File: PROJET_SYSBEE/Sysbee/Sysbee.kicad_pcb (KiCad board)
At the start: 2 copper layers, 64 x 58 mm, 47 parts, among them J1 Alim12V, J2 Connecteur Sim, J3 NO, J4 NE, J5 SO, J6 SE, J7 Connecteur programmation, J8 Micro_SD_Card_Det_Hirose_DM3AT, J9 Conn_01x03, U1 STM32L073CZTx, U2 LT1764, U3 AP1117-33, U4 ADS1231

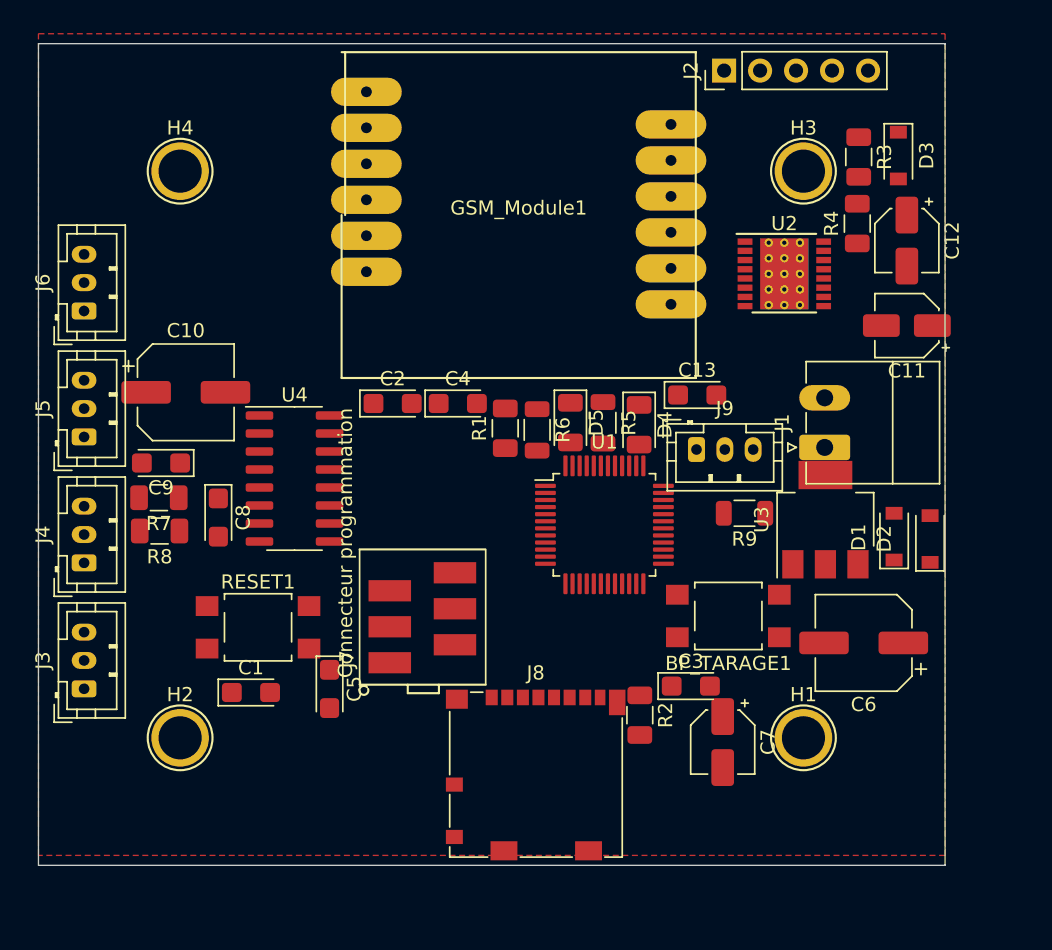
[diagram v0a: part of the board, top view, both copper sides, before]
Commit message: placement et routage, reste à redessiner un peu les pistes et rajouter les écritures F.Silks
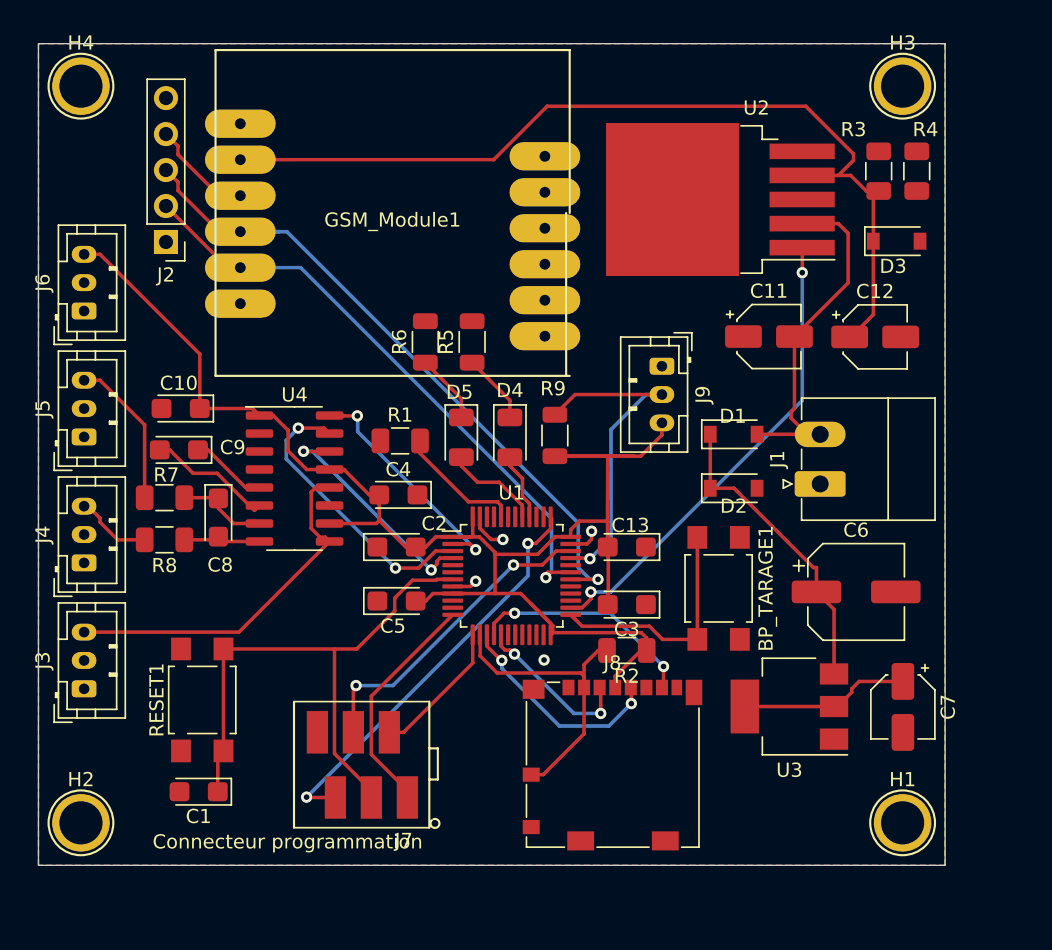
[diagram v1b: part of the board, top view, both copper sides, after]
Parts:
- C10: footprint Capacitor_SMD:CP_Elec_6.3x5.4 -> Capacitor_Tantalum_SMD:CP_EIA-3216-18_Kemet-A
- U2: value LT1764 -> MIC29302WU; footprint Package_SO:HTSSOP-16-1EP_4.4x5mm_P0.65mm_EP3.4x5mm_Mask3x3mm_ThermalVias -> Package_TO_SOT_SMD:TO-263-5_TabPin3
- moved J2 41.2 mm to (49.0, 44.0), turned to 180 degrees
- moved J7 15.9 mm to (59.7, 81.9), turned to 180 degrees
- moved R9 14.5 mm to (76.5, 57.7), turned to 90 degrees
- moved D2 14.3 mm to (89.1, 61.4), turned to 0 degrees
- moved D1 13.4 mm to (89.1, 57.6), turned to 0 degrees
- moved U3 13.4 mm to (93.0, 76.8), turned to 180 degrees
- moved C7 13.0 mm to (101.0, 76.8)
- moved C13 11.8 mm to (81.5, 65.5), turned to 180 degrees
- moved R5 10.9 mm to (70.6, 51.1), turned to 90 degrees
- moved C2 10.1 mm to (65.3, 65.5)
- moved R6 10.0 mm to (67.3, 51.1), turned to 90 degrees
- moved C11 9.76 mm to (91.6, 50.7), turned to 0 degrees
- moved H1 9.22 mm to (101.0, 85.0)
- moved H2 9.22 mm to (43.0, 85.0)
- moved H3 9.22 mm to (101.0, 33.0)
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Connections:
- C13 pad 1: Net-(C13-Pad1) -> GND
- C13 pad 2: /Alim/3,3V -> /E+
- C2 pad 1: Net-(C2-Pad1) -> GND
- C2 pad 2: /Alim/3,3V -> /E+
- C3 pad 1: Net-(C3-Pad1) -> GND
- C3 pad 2: /Alim/3,3V -> /E+
- C4 pad 1: Net-(C4-Pad1) -> GND
- C4 pad 2: /Alim/3,3V -> /E+
- C5 pad 1: Net-(C5-Pad1) -> GND
- C5 pad 2: /Alim/3,3V -> /E+
- C7 pad 1: /Alim/3,3V -> /E+
- J8 pad 4: /Alim/3,3V -> /E+
- J8 pad 7: /Microcontrôleur/SPI_MOSI -> /Microcontrôleur/SPI_MISO
- J9 pad 3: /Alim/3,3V -> /E+
- R2 pad 1: /Alim/3,3V -> /E+
- R9 pad 1: /Alim/3,3V -> /E+
- U1 pad 1: Net-(C2-Pad1) -> /E+
- U1 pad 14: /Microcontrôleur/SPI_SS -> /Microcontrôleur/SD_CS
- U1 pad 21: /Microcontrôleur/SD_CS -> Net-(U1-Pad21)
- U1 pad 24: Net-(C3-Pad1) -> /E+
- U1 pad 36: Net-(C13-Pad1) -> /E+
- U1 pad 48: Net-(C4-Pad1) -> /E+
- U1 pad 9: Net-(C5-Pad1) -> /E+
- U2 pad 1: GND -> /Alim/GSM_SHDN
- U2 pad 2: Net-(U2-Pad2) -> /Alim/12V
- U2 pad 3: /Alim/3,9V -> GND
- U2 pad 5: /Alim/3,9V -> Net-(R3-Pad2)
- U3 pad 2: /Alim/3,3V -> /E+
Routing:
- net /E+: track 0.00 -> 130.1 mm
- net /Alim/3,9V: track 0.00 -> 64.9 mm
- net /GSM_RX: track 0.00 -> 49.3 mm, vias 0 -> 1
- net /GSM_TX: track 0.00 -> 42.7 mm, vias 0 -> 1
- net /Microcontrôleur/NRST: track 0.00 -> 40.5 mm
- net /Alim/GSM_SHDN: track 0.00 -> 35.3 mm, vias 0 -> 2
- net /Microcontrôleur/SWCLK: track 0.00 -> 29.3 mm, vias 0 -> 2
- net /ADS1231/E-: track 0.00 -> 25.7 mm
- net /Alim/12V: track 0.00 -> 25.2 mm
- net /Microcontrôleur/TEMP: track 0.00 -> 23.9 mm, vias 0 -> 1
- net /Microcontrôleur/SWDON: track 0.00 -> 22.5 mm, vias 0 -> 2
- net /Microcontrôleur/SD_CS: track 0.00 -> 22.1 mm
- net Net-(C6-Pad1): track 0.00 -> 21.6 mm
- net /ADS1231/PD_SCK: track 0.00 -> 20.7 mm, vias 0 -> 2
- net /ADS1231/DOUT: track 0.00 -> 17.6 mm, vias 0 -> 2
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- added copper zone on B.Cu, net GND

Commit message: placement et routage ok
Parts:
- added G***: LOGO, Logos:logo_riot_os, F.Cu at (147.4, 75.4)
- added G***: LOGO, Logos:logo_riot_os, B.Cu at (138.8, 117.8)
- added G***: LOGO, Logos:logo_iut_cachan_FrontSilk, F.Cu at (155.1, 93.2)
- added REF**: KiCad-Logo2_5mm_SilkScreen, Symbol:KiCad-Logo2_5mm_SilkScreen, B.Cu at (171.5, 75.9)
- GSM_SIM800L1: renamed from GSM_Module1; value SIM800L -> GSM_SIM800L
- J2: value Connecteur Sim -> SIM800L DEBUG
- J7: value Connecteur programmation -> Conn Prog STLINKV2
- J8: value Micro_SD_Card_Det_Hirose_DM3AT -> Micro_SD
- R3: value 4,7k -> 430
- R4: value 4,7k -> 200
- RESET1: value SW_Push -> Reset
- moved C1 91.4 mm to (133.8, 122.2)
- moved R3 91.4 mm to (181.8, 78.4)
- moved C10 91.4 mm to (132.5, 95.2)
- moved C11 91.4 mm to (174.0, 90.1)
- moved C13 91.4 mm to (164.0, 105.0)
- moved C2 91.4 mm to (147.7, 105.0)
- moved C5 91.4 mm to (147.7, 108.8)
- moved C7 91.4 mm to (183.5, 116.2)
- moved C8 91.4 mm to (135.1, 102.9)
- moved D1 91.4 mm to (171.5, 97.0)
- moved D2 91.4 mm to (171.5, 100.8)
- moved H2 91.4 mm to (125.4, 124.4)
- moved H4 91.4 mm to (125.4, 72.4)
- moved J3 91.4 mm to (125.7, 115.0)
- moved J4 91.4 mm to (125.7, 106.1)
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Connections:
- net /ADS1231/PWDRN renamed /ADS1231/ADC_PWDRN
- C12 pad 1: /Alim/3,9V -> /3,9V
- D3 pad 1: /Alim/3,9V -> /3,9V
- GSM_SIM800L1 pad 2: /Alim/3,9V -> /3,9V
- J1 pad 1: GND -> /Alim/12V
- J1 pad 2: /Alim/12V -> GND
- J7 pad 1: /Microcontrôleur/UART_TX -> /Microcontrôleur/UART_RX
- J7 pad 2: /Microcontrôleur/UART_RX -> /Microcontrôleur/UART_TX
- J7 pad 3: /Microcontrôleur/NRST -> /Microcontrôleur/SWDIO
- J7 pad 4: /Microcontrôleur/SWDON -> /Microcontrôleur/SWCLK
- J7 pad 5: /Microcontrôleur/SWCLK -> /Microcontrôleur/NRST
- R3 pad 1: /Alim/3,9V -> /3,9V
- U1 pad 2: /ADS1231/DOUT -> /Microcontrôleur/ADC_DOUT
- U1 pad 3: /ADS1231/PD_SCK -> /Microcontrôleur/ADC_CLK
- U1 pad 34: /Microcontrôleur/SWDON -> /Microcontrôleur/SWDIO
- U2 pad 4: /Alim/3,9V -> /3,9V
- U4 pad 15: /ADS1231/PD_SCK -> /ADS1231/ADC_CLK
- U4 pad 16: /ADS1231/DOUT -> /ADS1231/ADC_DOUT
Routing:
- net /3,9V: track 0.00 -> 80.2 mm
- net /Alim/3,9V: track 64.9 -> 0.00 mm
- net /Microcontrôleur/SWDIO: track 0.00 -> 24.9 mm, vias 0 -> 2
- net /E+: track 130.1 -> 153.8 mm
- net /Microcontrôleur/SWDON: track 22.5 -> 0.00 mm, vias 2 -> 0
- net /ADS1231/PD_SCK: track 20.7 -> 0.00 mm, vias 2 -> 0
- net Net-(J4-Pad1): track 0.00 -> 19.4 mm
- net Net-(J3-Pad1): track 0.00 -> 19.0 mm
- net /ADS1231/DOUT: track 17.6 -> 0.00 mm, vias 2 -> 0
- net Net-(J3-Pad2): track 0.00 -> 12.1 mm
- net Net-(J5-Pad2): track 0.00 -> 11.8 mm
- net /Microcontrôleur/SPI_MOSI: track 11.7 -> 20.2 mm, vias 2 -> 0
- net Net-(R3-Pad2): track 0.00 -> 8.09 mm
- net /Microcontrôleur/SD_CS: track 22.1 -> 29.8 mm, vias 0 -> 2
- net /Microcontrôleur/SWCLK: track 29.3 -> 21.8 mm
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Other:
- board text added: "+12V"
- board text added: "+3.3V"
- board text added: "1"
- board text added: "1-Wire : PA12"
- board text added: "1-wire"
- board text added: "3.9V"
- board text added: "ADC_PWR_DOWN : PC15"
- board text added: "BP Tare : PB12"
- board text added: "GND"
- board text added: "GSM_RST"
- board text added: "GSM_RX"
- board text added: "GSM_TX"
- board text added: "J. SelvaKumaran L. NDede-Epee T. Perchoc D. Pénard 03-2021"
- board text added: "LED_R"
- board text added: "LED_R : PB4"
- board text added: "LED_V"
- board text added: "LED_V : PB5"
- board text added: "NE"
- board text added: "NO"
- board text added: "NRST"
- board text added: "SE"
- board text added: "SO"
- board text added: "STM32L073RZ"
- board text added: "SWCLK"
- board text added: "SWDIO"
- board text added: "Sonde Température DS18B20"
- board text added: "UART_RX"
- board text added: "UART_TX"
- board text added: "VCC"
- board text removed: "Ne pas oublier capteur temp (cahier)"
